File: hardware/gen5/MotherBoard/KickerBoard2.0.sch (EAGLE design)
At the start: 155 parts

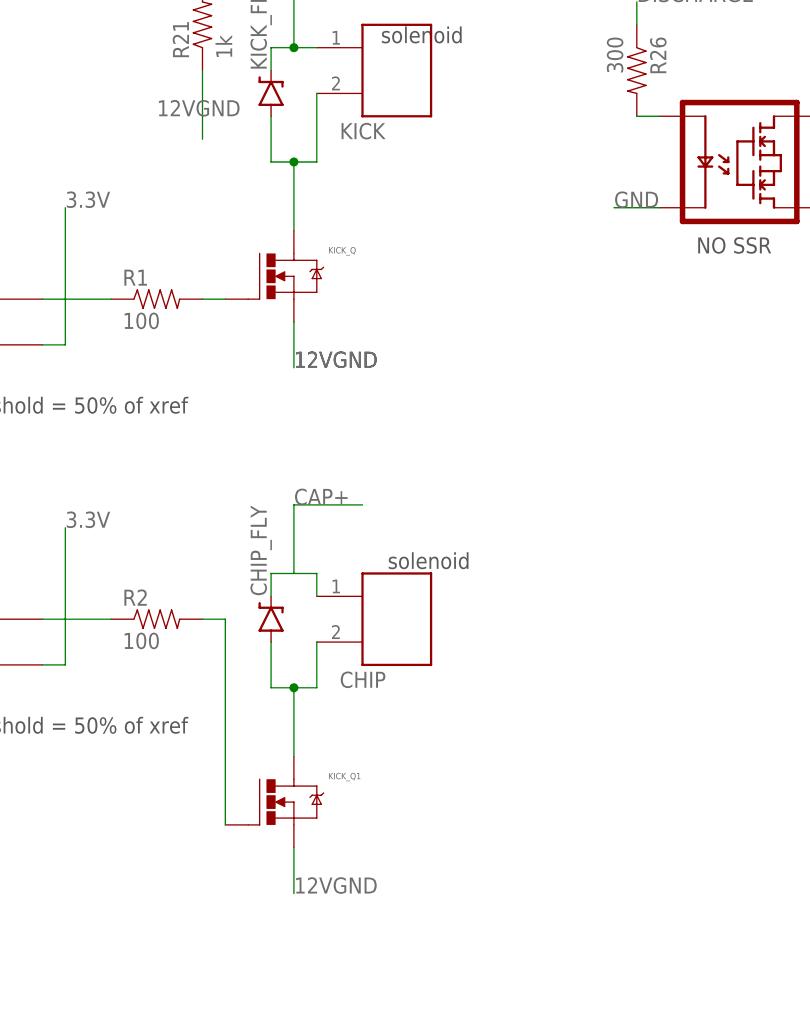
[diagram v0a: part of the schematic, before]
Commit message: added big ol' transistors
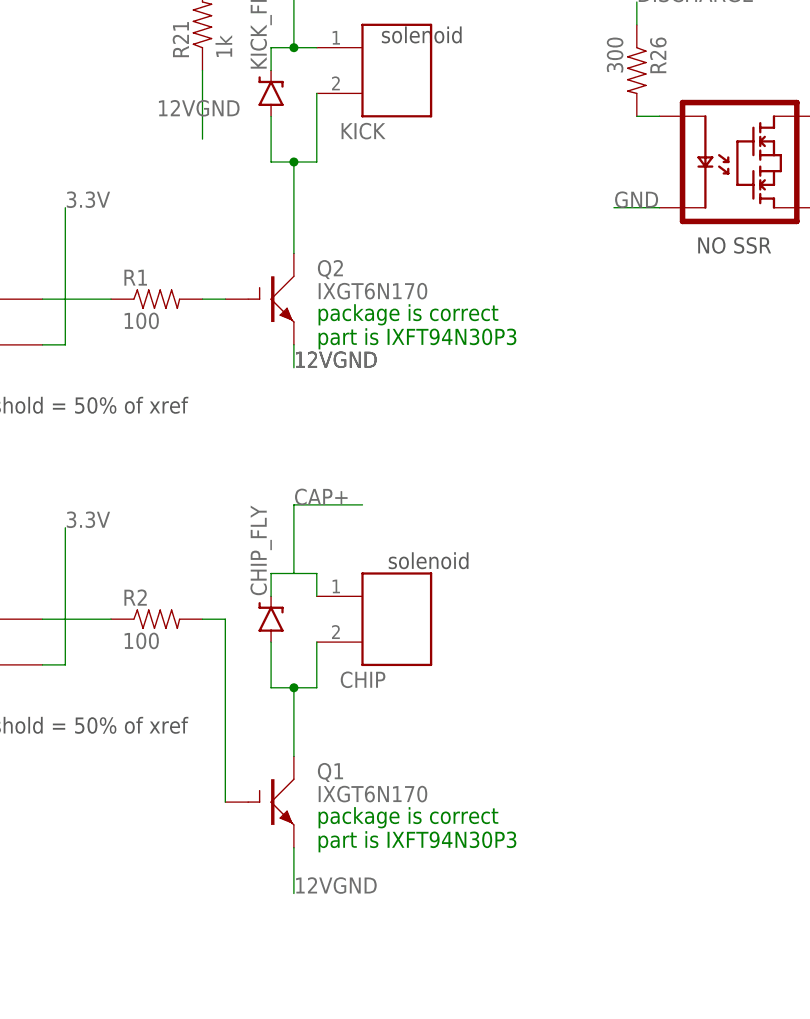
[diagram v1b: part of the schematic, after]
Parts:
- removed KICK_Q, KICK_Q1: (no value), gen3:N-MOSFETDPAK
- added Q1, Q2: IXGT6N170, transistor-power:IXGT6N170
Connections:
- net 12VGND: now also Q1.E, Q2.E; no longer KICK_Q.S, KICK_Q1.S
- net LOWCHIP: now also Q1.C; no longer KICK_Q1.D
- net LOWKICK: now also Q2.C; no longer KICK_Q.D
- net N$3: now also Q1.G; no longer KICK_Q1.G
- net N$8: now also Q2.G; no longer KICK_Q.G
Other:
- note added: "package is correct part is IXFT94N30P3"

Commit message: moved connector to edge, replaced transistors, routed
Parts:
- removed Q1: IXGT6N170, transistor-power:IXGT6N170
- added Q3: IXFH6N90, transistor-power:IXFH6N90
- Q2: value IXGT6N170 -> IXFH6N90; device transistor-power:IXGT6N170 -> transistor-power:IXFH6N90
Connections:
- net 12VGND: now also Q2.S, Q3.S; no longer Q1.E, Q2.E
- net 3.3V: now also J1.7, J2.7, J3.3, J4.3
- net LOWCHIP: now also Q2.D; no longer Q1.C
- net LOWKICK: now also Q3.D; no longer Q2.C
- net N$3: now also Q2.G; no longer Q1.G
- net N$8: now also Q3.G; no longer Q2.G
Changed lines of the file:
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@@
 <part name="U$9" library="Kicker" deviceset="MOTOR_BOARD" device=""/>
 <part name="U$10" library="Kicker" deviceset="MOTOR_BOARD" device=""/>
-<part name="Q1" library="transistor-power" library_urn="urn:adsk.eagle:library:400" deviceset="IXG?*N170" device="T" package3d_urn="urn:adsk.eagle:package:29509/1" technology="6"/>
-<part name="Q2" library="transistor-power" library_urn="urn:adsk.eagle:library:400" deviceset="IXG?*N170" device="T" package3d_urn="urn:adsk.eagle:package:29509/1" technology="6"/>
+<part name="Q3" library="transistor-power" library_urn="urn:adsk.eagle:library:400" deviceset="IXF?6N*" device="H" package3d_urn="urn:adsk.eagle:package:29508/1" technology="90"/>
+<part name="Q2" library="transistor-power" library_urn="urn:adsk.eagle:library:400" deviceset="IXF?6N*" device="H" package3d_urn="urn:adsk.eagle:package:29508/1" technology="90"/>
 </parts>
 <sheets>
@@
 <wire x1="327.66" y1="248.92" x2="261.62" y2="248.92" width="0.1524" layer="97"/>
 <wire x1="261.62" y1="248.92" x2="261.62" y2="190.5" width="0.1524" layer="97"/>
-<text x="485.14" y="304.8" size="1.778" layer="91">package is correct
+<text x="487.68" y="307.34" size="1.778" layer="91">package is correct
 part is IXFT94N30P3</text>
-<text x="485.14" y="248.92" size="1.778" layer="91">package is correct
+<text x="487.68" y="248.92" size="1.778" layer="91">package is correct
 part is IXFT94N30P3</text>
 </plain>
@@
 <instance part="U$9" gate="G$1" x="223.52" y="261.62" smashed="yes" rot="R90"/>
 <instance part="U$10" gate="G$1" x="223.52" y="330.2" smashed="yes" rot="R90"/>
-<instance part="Q1" gate="G$1" x="480.06" y="254" smashed="yes">
-<attribute name="NAME" x="485.14" y="256.54" size="1.778" layer="95"/>
-<attribute name="VALUE" x="485.14" y="254" size="1.778" layer="96"/>
-</instance>
-<instance part="Q2" gate="G$1" x="480.06" y="309.88" smashed="yes">
-<attribute name="NAME" x="485.14" y="312.42" size="1.778" layer="95"/>
-<attribute name="VALUE" x="485.14" y="309.88" size="1.778" layer="96"/>
+<instance part="Q3" gate="G$1" x="480.06" y="312.42" smashed="yes">
+<attribute name="NAME" x="487.68" y="314.96" size="1.778" layer="95"/>
+<attribute name="VALUE" x="487.68" y="312.42" size="1.778" layer="96"/>
+</instance>
+<instance part="Q2" gate="G$1" x="480.06" y="254" smashed="yes">
+<attribute name="NAME" x="487.68" y="256.54" size="1.778" layer="95"/>
+<attribute name="VALUE" x="487.68" y="254" size="1.778" layer="96"/>
 </instance>
 </instances>
@@
 <wire x1="416.56" y1="124.46" x2="406.4" y2="124.46" width="0.1524" layer="91"/>
 <label x="406.4" y="124.46" size="1.778" layer="95"/>
+</segment>
+<segment>
+<pinref part="J1" gate="G$1" pin="7"/>
+<wire x1="139.7" y1="353.06" x2="139.7" y2="342.9" width="0.1524" layer="91"/>
+<label x="139.7" y="342.9" size="1.778" layer="95" rot="R90"/>
+</segment>
+<segment>
+<pinref part="J2" gate="G$1" pin="7"/>
+<wire x1="187.96" y1="353.06" x2="187.96" y2="342.9" width="0.1524" layer="91"/>
+<label x="187.96" y="342.9" size="1.778" layer="95" rot="R90"/>
+</segment>
+<segment>
+<pinref part="J4" gate="G$1" pin="3"/>
+<wire x1="139.7" y1="304.8" x2="139.7" y2="294.64" width="0.1524" layer="91"/>
+<label x="139.7" y="294.64" size="1.778" layer="95" rot="R90"/>
+</segment>
+<segment>
+<pinref part="J3" gate="G$1" pin="3"/>
+<wire x1="187.96" y1="302.26" x2="187.96" y2="294.64" width="0.1524" layer="91"/>
+<label x="187.96" y="294.64" size="1.778" layer="95" rot="R90"/>
 </segment>
 </net>
@@
 <wire x1="482.6" y1="248.92" x2="482.6" y2="243.84" width="0.1524" layer="91"/>
 <label x="482.6" y="243.84" size="1.778" layer="95"/>
-<pinref part="Q1" gate="G$1" pin="E"/>
-</segment>
-<segment>
-<wire x1="482.6" y1="304.8" x2="482.6" y2="302.26" width="0.1524" layer="91"/>
+<pinref part="Q2" gate="G$1" pin="S"/>
+</segment>
+<segment>
 <label x="482.6" y="302.26" size="1.778" layer="95"/>
 <label x="482.6" y="302.26" size="1.778" layer="95"/>
-<pinref part="Q2" gate="G$1" pin="E"/>
+<pinref part="Q3" gate="G$1" pin="S"/>
+<wire x1="482.6" y1="307.34" x2="482.6" y2="302.26" width="0.1524" layer="91"/>
 </segment>
 <segment>
@@
 <pinref part="R2" gate="G$1" pin="2"/>
 <wire x1="472.44" y1="274.32" x2="474.98" y2="274.32" width="0.1524" layer="91"/>
-<wire x1="474.98" y1="274.32" x2="474.98" y2="254" width="0.1524" layer="91"/>
-<pinref part="Q1" gate="G$1" pin="G"/>
+<wire x1="474.98" y1="274.32" x2="474.98" y2="251.46" width="0.1524" layer="91"/>
+<pinref part="Q2" gate="G$1" pin="G"/>
+<wire x1="477.52" y1="251.46" x2="474.98" y2="251.46" width="0.1524" layer="91"/>
 </segment>
 </net>
@@
 <wire x1="482.6" y1="266.7" x2="482.6" y2="259.08" width="0.1524" layer="91"/>
 <junction x="482.6" y="266.7"/>
-<pinref part="Q1" gate="G$1" pin="C"/>
+<pinref part="Q2" gate="G$1" pin="D"/>
 </segment>
 </net>
@@
 <pinref part="R1" gate="G$1" pin="2"/>
 <wire x1="474.98" y1="309.88" x2="472.44" y2="309.88" width="0.1524" layer="91"/>
-<pinref part="Q2" gate="G$1" pin="G"/>
+<pinref part="Q3" gate="G$1" pin="G"/>
+<wire x1="477.52" y1="309.88" x2="472.44" y2="309.88" width="0.1524" layer="91"/>
 </segment>
 </net>
@@
 <wire x1="482.6" y1="325.12" x2="485.14" y2="325.12" width="0.1524" layer="91"/>
 <junction x="482.6" y="325.12"/>
-<wire x1="482.6" y1="325.12" x2="482.6" y2="314.96" width="0.1524" layer="91"/>
-<pinref part="Q2" gate="G$1" pin="C"/>
-</segment>
-</net>
+<wire x1="482.6" y1="325.12" x2="482.6" y2="317.5" width="0.1524" layer="91"/>
+<pinref part="Q3" gate="G$1" pin="D"/>
+<wire x1="482.6" y1="317.5" x2="482.6" y2="314.96" width="0.1524" layer="91"/>
+</segment>
+</net>

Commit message: new motor controller
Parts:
- added U$16: VNH5019, IAD-Library:VNH5019
- added U$20: MOSFET-NCH, IAD-Library:MOSFET-NCH
